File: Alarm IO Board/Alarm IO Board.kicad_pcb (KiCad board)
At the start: 2 copper layers, 75 x 100 mm, 48 parts, among them J1 Conn_02x10_Odd_Even, J2 Conn_01x02_Socket, SW1 Wurth WS-TATV, SW2 Wurth WS-TATV, SW3 Wurth WS-TATV, SW4 Wurth WS-TATV, SW5 Wurth WS-TATV, SW6 Wurth WS-TATV, U1 SN74LVC1G132, U10 TLV61046ADB, U2 TPL7407LA, U3 DRV8837C, U4 TPL7407LA, U5 TCA9535PWR, U6 OPT4048, U7 AD5274BRMZ-100, U8 TPS7A0525PDBV, U9 SN74LVC1G132

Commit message: Update IO board
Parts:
- removed R10, R11, R12, R13, R2, R3, R4, R5, R6, R7, R8, R9: 100k, Resistor_SMD:R_0603_1608Metric_Pad0.98x0.95mm_HandSolder
- removed U5: TCA9535PWR, Package_SO:TSSOP-24_4.4x7.8mm_P0.65mm
- added C14: 0u1, Capacitor_SMD:C_0603_1608Metric_Pad1.08x0.95mm_HandSolder, F.Cu at (160.1, 69.5)
- added C15: 0u1, 50V, Capacitor_SMD:C_0603_1608Metric_Pad1.08x0.95mm_HandSolder, F.Cu at (160.1, 72.0)
- added C16: 0u1, 50V, Capacitor_SMD:C_0603_1608Metric_Pad1.08x0.95mm_HandSolder, F.Cu at (160.1, 74.5)
- added C17: 0u1, 50V, Capacitor_SMD:C_0603_1608Metric_Pad1.08x0.95mm_HandSolder, F.Cu at (160.1, 77.0)
- added C18: 0u1, 50V, Capacitor_SMD:C_0603_1608Metric_Pad1.08x0.95mm_HandSolder, F.Cu at (160.1, 79.5)
- added H1: MountingHole_Pad, MountingHole:MountingHole_3.2mm_M3_Pad, F.Cu at (133.0, 59.0)
- added H2: MountingHole_Pad, MountingHole:MountingHole_3.2mm_M3_Pad, F.Cu at (61.0, 59.0)
- added H3: MountingHole_Pad, MountingHole:MountingHole_3.2mm_M3_Pad, F.Cu at (61.0, 115.0)
- added H4: MountingHole_Pad, MountingHole:MountingHole_3.2mm_M3_Pad, F.Cu at (133.0, 115.0)
- added R17: 470R, Resistor_SMD:R_0603_1608Metric_Pad0.98x0.95mm_HandSolder, F.Cu at (160.1, 82.0)
- added U11: TLV1824, kicad global library:SOT-23-THIN-14_2x4.2mm_P0.5_TI-DYY_HandSoldering, F.Cu at (99.0, 104.0)
- added U12: TLV1824, kicad global library:SOT-23-THIN-14_2x4.2mm_P0.5_TI-DYY_HandSoldering, F.Cu at (107.0, 104.2)
- added U13: TCA9555PWR, Package_SO:TSSOP-24_4.4x7.8mm_P0.65mm, F.Cu at (129.4, 102.4)
- added VFD1: IVL2-7/5, kicad global library:IVL2-75, F.Cu at (95.7, 84.5)
- J2: moved to B.Cu
- U2, U4: value TPL7407LA -> TLV1824; footprint Package_SO:TSSOP-16_4.4x5mm_P0.65mm -> kicad global library:SOT-23-THIN-14_2x4.2mm_P0.5_TI-DYY_HandSoldering
- moved J2 84.4 mm to (114.0, 81.5), turned to 180 degrees
- moved U6 72.3 mm to (61.0, 92.2)
- moved U2 60.9 mm to (91.0, 104.2)
- moved U4 58.8 mm to (84.0, 104.0)
- moved R1 54.3 mm to (36.6, 68.4), turned to 0 degrees
- moved C1 49.7 mm to (110.9, 64.6)
- moved C10 49.7 mm to (106.3, 61.9)
- moved C11 49.7 mm to (112.0, 59.6)
- moved C12 49.7 mm to (115.3, 59.6)
- moved C3 49.7 mm to (110.9, 66.2)
- moved U1 49.7 mm to (109.1, 62.0)
- moved U3 49.7 mm to (113.8, 65.3)
- moved C8 49.7 mm to (121.5, 63.1)
- moved C9 49.7 mm to (117.9, 65.9)
- moved R14 49.7 mm to (108.7, 59.6)
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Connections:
- J1 pad 4: unconnected-(J1-Pin_4-Pad4) -> GND
- U2 pad 1: /g -> /b_HV
- U2 pad 10: /a_HV -> /COMP_REF
- U2 pad 11: /b_HV -> /d
- U2 pad 12: /c_HV -> GND
- U2 pad 14: /e_HV -> /c_HV
- U2 pad 2: /f -> /a_HV
- U2 pad 3: /e -> +VSW
- U2 pad 4: /d -> /COMP_REF
- U2 pad 5: /c -> /a
- U2 pad 6: /b -> /COMP_REF
- U2 pad 7: /a -> /b
- U2 pad 8: GND -> /COMP_REF
- U2 pad 9: +VSW -> /c
- U4 pad 1: /1 -> /f_HV
- U4 pad 10: unconnected-(U4-O7-Pad10) -> /COMP_REF
- U4 pad 11: unconnected-(U4-O6-Pad11) -> /sep_top
- U4 pad 12: /sep_HV -> GND
- U4 pad 13: /4_HV -> /sep_top_HV
- U4 pad 14: /3_HV -> /g_HV
- U4 pad 2: /2 -> /e_HV
- U4 pad 3: /3 -> +VSW
- U4 pad 4: /4 -> /COMP_REF
- U4 pad 5: /sep -> /e
- U4 pad 6: GND -> /COMP_REF
- U4 pad 7: GND -> /f
- U4 pad 8: GND -> /COMP_REF
- U4 pad 9: +VSW -> /g
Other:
- board size 75 x 100 mm -> 80 x 65 mm

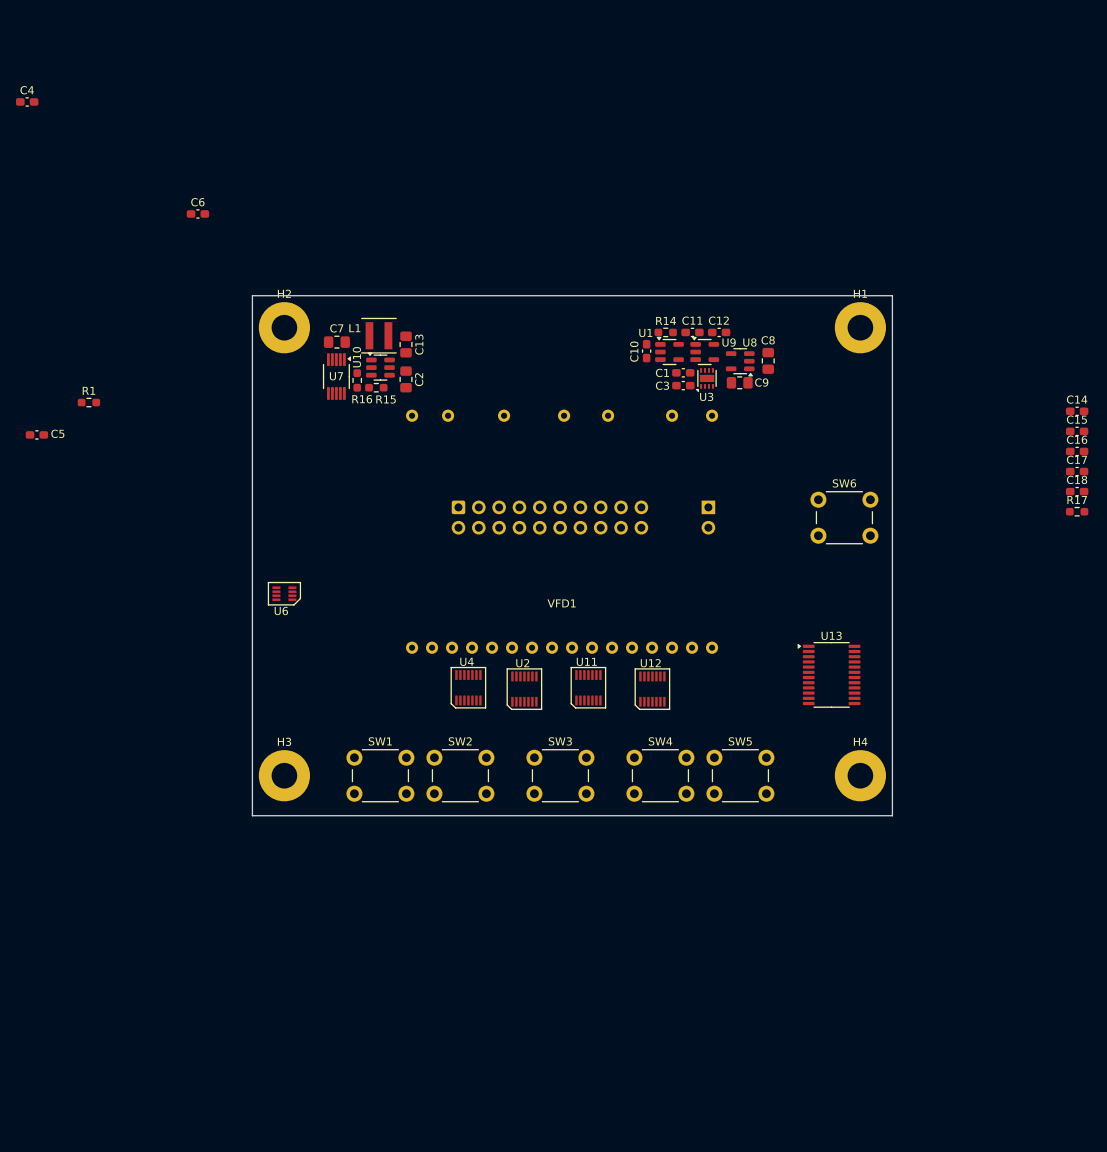
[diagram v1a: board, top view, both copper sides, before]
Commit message: Finish IO board
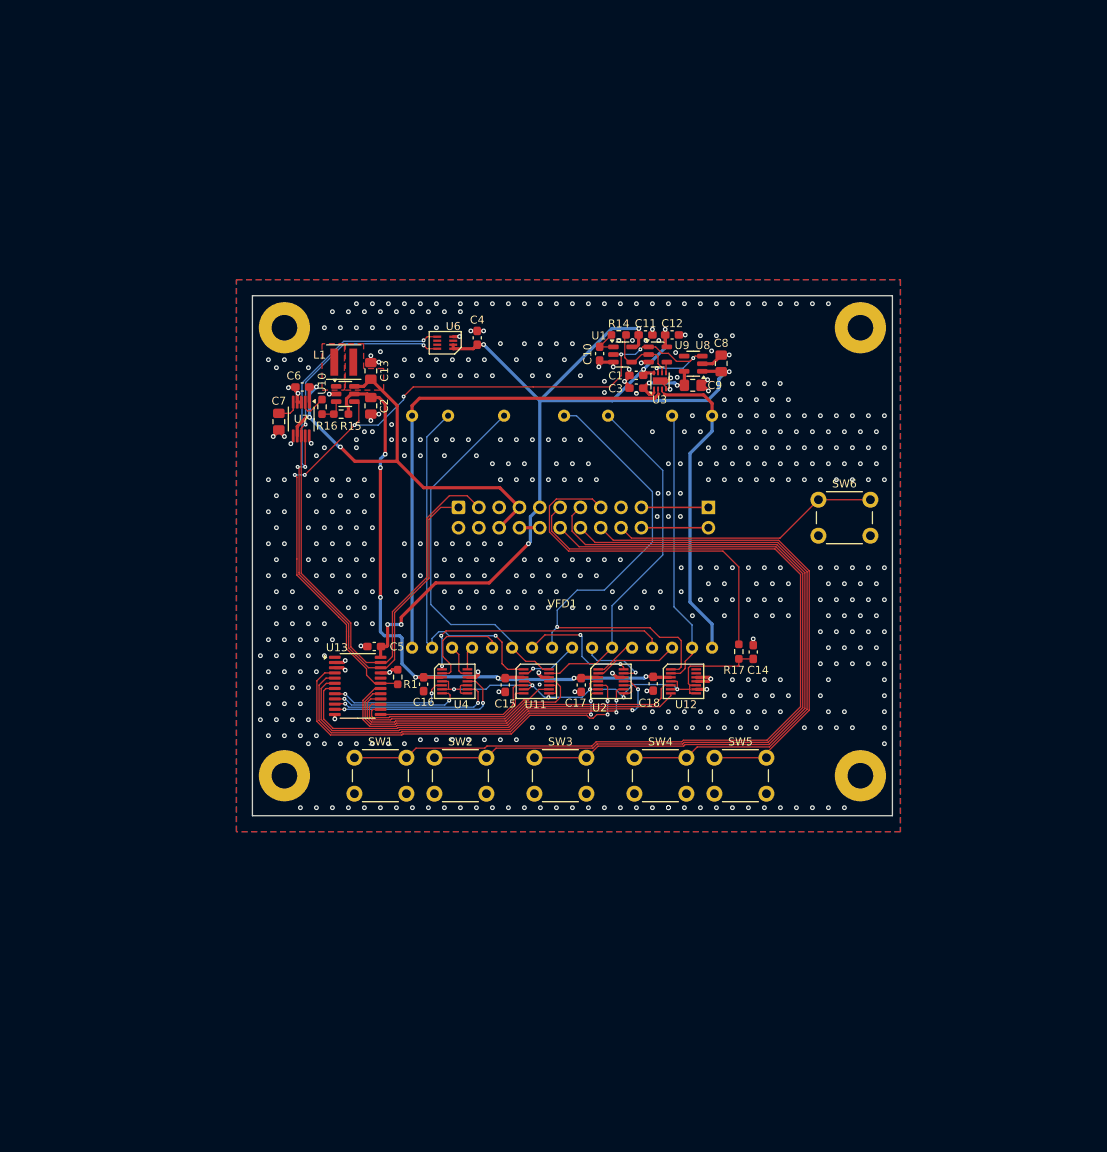
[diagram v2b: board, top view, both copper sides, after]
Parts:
- moved C16 86.7 mm to (78.4, 103.6), turned to -90 degrees
- moved C15 78.2 mm to (88.6, 103.7), turned to -90 degrees
- moved C17 67.5 mm to (98.1, 103.7), turned to -90 degrees
- moved C4 63.5 mm to (85.1, 60.3), turned to 90 degrees
- moved U13 59.3 mm to (70.2, 103.8)
- moved C18 58.2 mm to (107.1, 103.5), turned to -90 degrees
- moved R1 51.6 mm to (75.2, 102.7), turned to 90 degrees
- moved C14 50.4 mm to (119.6, 99.5), turned to 90 degrees
- moved C5 49.8 mm to (72.2, 98.8), turned to 180 degrees
- moved R17 45.8 mm to (117.8, 99.5), turned to 90 degrees
- moved U6 37.3 mm to (81.1, 60.9)
- moved C6 25.3 mm to (63.2, 66.4), turned to 180 degrees
- moved C7 12.3 mm to (60.3, 70.7), turned to -90 degrees
- moved U2 10.9 mm to (101.8, 103.2), turned to -90 degrees
- moved U7 6.90 mm to (63.1, 70.4)
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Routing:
- net +3V3: track 0.00 -> 124.8 mm, vias 0 -> 8
- net /SWI1: track 0.00 -> 111.7 mm
- net /disp_En: track 0.00 -> 103.8 mm, vias 0 -> 8
- net /SWI2: track 0.00 -> 98.1 mm
- net /I2C_SCL: track 0.00 -> 90.9 mm, vias 0 -> 3
- net /I2C_SDA: track 0.00 -> 88.3 mm, vias 0 -> 2
- net /SWI3: track 0.00 -> 88.0 mm
- net +VSW: track 0.00 -> 86.9 mm, vias 0 -> 7
- net /SWI4: track 0.00 -> 71.9 mm
- net /COMP_REF: track 0.00 -> 67.3 mm, vias 0 -> 6
- net /sep_HV: track 0.00 -> 62.6 mm, vias 0 -> 1
- net /VFa: track 0.00 -> 62.4 mm
- net /AIN1: track 0.00 -> 60.4 mm
- net +5V: track 0.00 -> 58.7 mm, vias 0 -> 3
- net GND: track 0.00 -> 53.2 mm, vias 0 -> 540
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- added copper zone on F.Cu, net +5V
- added copper zone on F.Cu, net /VFD Power/BOOST_SW
- added copper zone on B.Cu, net GND
- added copper zone on F.Cu, net GND
